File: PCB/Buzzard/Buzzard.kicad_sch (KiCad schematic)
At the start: 69 parts, among them J1 PJ-320A, J2 SDA, J3 SCL, J4 Haptic Buzz, J5 TrackPoint, J6 OLED, J7 LCD, J8 Battery, SW1 SW_DPST_x2, SW2 Reset, U1 ProMicro

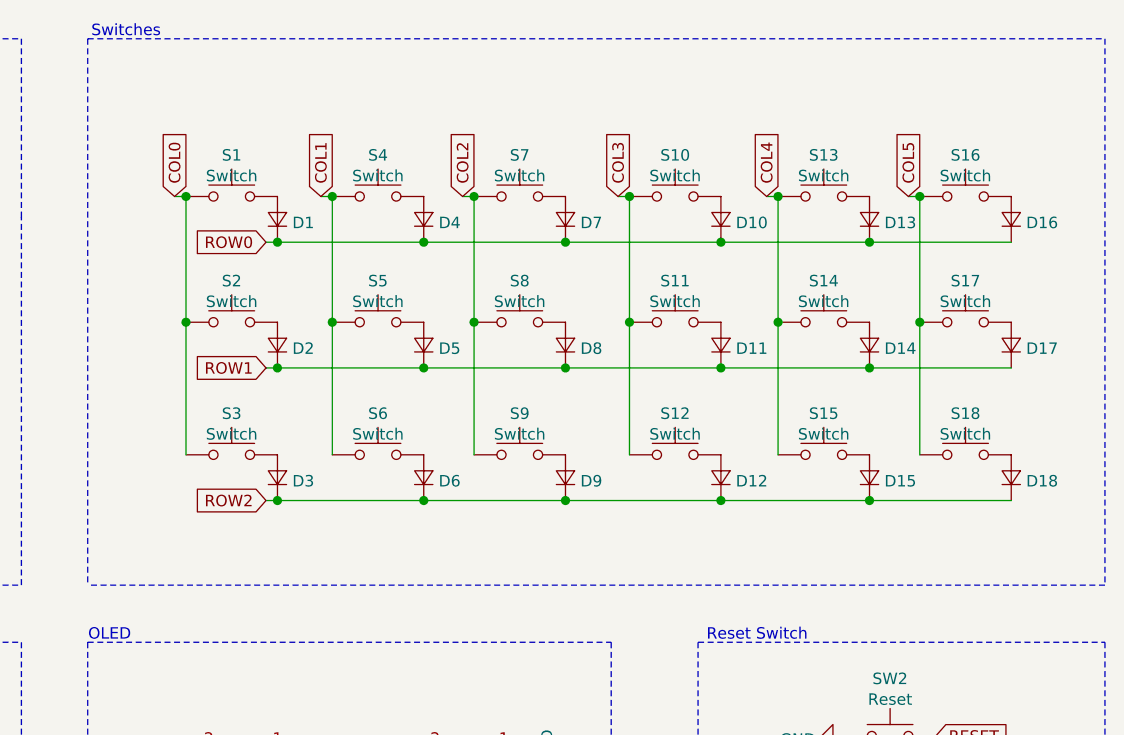
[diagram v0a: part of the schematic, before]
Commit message: started with pcb design and placed switches
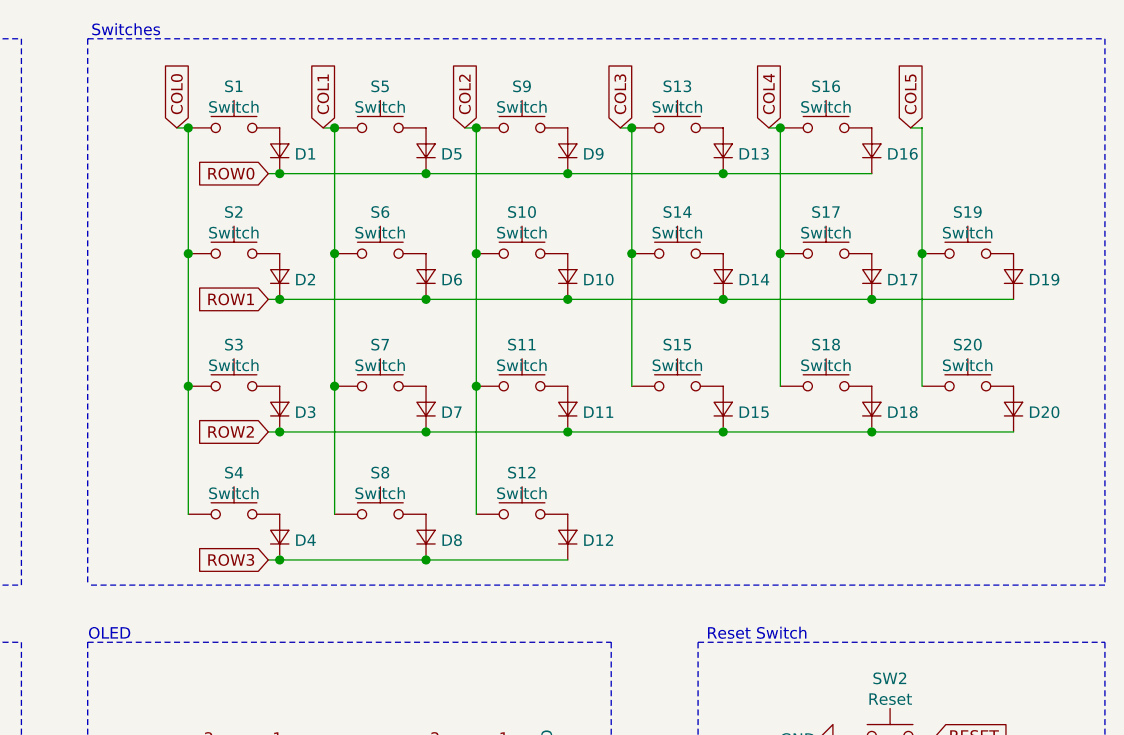
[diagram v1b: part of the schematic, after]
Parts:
- removed D18: D_Small, Buzzard:D3_TH_SMD_v2, symbol Device:D_Small
- removed S18: Switch, Buzzard:Kailh_socket_PG1350_optional_reversible.kicad_mod, symbol Switch:SW_Push
- added D12, D4, D8: D_Small, Buzzard:D3_TH_SMD_v2, symbol Device:D_Small
- added S12, S4, S8: Switch, Buzzard:Kailh_socket_PG1350_optional_reversible.kicad_mod, symbol Switch:SW_Push
- renumbered D8 to D10, D9 to D11, D10 to D13, D11 to D14, D12 to D15, D13 to D16, D14 to D17, D15 to D18, D16 to D19, D17 to D20, D4 to D5, D5 to D6, D6 to D7, D7 to D9, S8 to S10, S9 to S11, S10 to S13, S11 to S14, S12 to S15, S13 to S16, S14 to S17, S15 to S18, S16 to S19, S17 to S20, S4 to S5, S5 to S6, S6 to S7, S7 to S9
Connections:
- net COL0: now also S4.1
- net COL1: now also S8.1
- net COL2: now also S12.1
- net ROW0: no longer D19.1 (K)
- net ROW1: now also D19.1 (K); no longer D20.1 (K)
- net ROW2: now also D20.1 (K)
- net ROW3: now also D12.1 (K), D4.1 (K), D8.1 (K)
- new net: D8.2 (A), S8.2
- new net: D4.2 (A), S4.2
- new net: D12.2 (A), S12.2
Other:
- moved on the sheet: D1, D10, D11, D13, D14, D15, D16, D17, D18, D19, D2, D20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

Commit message: further work on pcb
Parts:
- J4: footprint Connector_PinHeader_1.00mm:PinHeader_1x05_P1.00mm_Vertical -> Buzzard:Pimoroni Haptic Buzz DRV2605L Driver
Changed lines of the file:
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@@
       (effects (font (size 1.27 1.27)) (justify left))
     )
-    (property "Footprint" "Connector_PinHeader_1.00mm:PinHeader_1x05_P1.00mm_Vertical" (id 2) (at 77.978 170.18 0)
+    (property "Footprint" "Buzzard:Pimoroni Haptic Buzz DRV2605L Driver" (id 2) (at 77.978 170.18 0)
       (effects (font (size 1.27 1.27)) hide)
     )
@@
     )
     (path "/15f956f5-7f0a-47a7-8d82-945c44e3054e"
-      (reference "J4") (unit 1) (value "Haptic Buzz") (footprint "Connector_PinHeader_1.00mm:PinHeader_1x05_P1.00mm_Vertical")
+      (reference "J4") (unit 1) (value "Haptic Buzz") (footprint "Buzzard:Pimoroni Haptic Buzz DRV2605L Driver")
     )
     (path "/c9007f78-8c46-454a-961b-6abc2490a937"

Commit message: further work on the pcb
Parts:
- removed J2: SDA, Connector_PinHeader_2.54mm:PinHeader_1x01_P2.54mm_Vertical, symbol Connector_Generic:Conn_01x01
- removed J3: SCL, Connector_PinHeader_2.54mm:PinHeader_1x01_P2.54mm_Vertical, symbol Connector_Generic:Conn_01x01
- removed J7: LCD, Connector_PinHeader_1.00mm:PinHeader_1x08_P1.00mm_Vertical, symbol Connector_Generic:Conn_01x09
- added J7: Sharp Memory LCD Breakout, Buzzard:SharpMemoryLcdBreakout-Reversable, symbol Connector_Generic:Conn_02x03_Odd_Even
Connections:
- net GND: now also J7.2 (Pin_2), J7.6 (Pin_6)
- net LCD_DI: now also J7.3 (Pin_3)
- net VCC: now also J7.4 (Pin_4)
- net at JP11.2 (B), JP12.2 (B): now also J7.5 (Pin_5)
- net at JP10.2 (B), JP9.2 (B): now also J7.1 (Pin_1)
- no-connect marks 2 -> 0

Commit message: further work
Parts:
- J7: symbol Connector_Generic:Conn_02x03_Odd_Even -> Connector_Generic:Conn_2Rows-05Pins
- S1, S10, S5, S6, S9: footprint Buzzard:Kailh_socket_PG1350_optional_reversible.kicad_mod -> Buzzard:SW_PG1350_reversible
- SW2: footprint Buzzard:SMD-SW-4_5.1x5.1x2.5 -> Buzzard:SW_Tactile_SPST_Angled_PTS645Vx39-2LFS
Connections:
- net GND: no longer J7.6 (Pin_6)
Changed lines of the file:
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@@
-    (pin "1")
-  )
-  (symbol (lib_id "power:GND") (at 159.004 171.45 90) (unit 1)
-    (in_bom yes) (on_board yes) (fields_autoplaced)
-    (property "Reference" "#PWR0101" (id 0) (at 165.354 171.45 0)
-      (effects (font (size 1.27 1.27)) hide)
-    )
-    (property "Value" "GND" (id 1) (at 162.1791 171.8385 90)
-      (effects (font (size 1.27 1.27)) (justify right))
-    )
-    (property "Footprint" "" (id 2) (at 159.004 171.45 0)
-      (effects (font (size 1.27 1.27)) hide)
-    )
-    (property "Datasheet" "" (id 3) (at 159.004 171.45 0)
-      (effects (font (size 1.27 1.27)) hide)
-    )
     (pin "1")
   )
@@
   (symbol (lib_id "Switch:SW_Push") (at 129.54 26.162 0) (unit 1)
     (in_bom yes) (on_board yes) (fields_autoplaced)
-    (property "Reference" "S1" (id 0) (at 129.54 21.5858 0))
-    (property "Value" "Switch" (id 1) (at 129.54 23.8845 0))
-    (property "Footprint" "Buzzard:Kailh_socket_PG1350_optional_reversible.kicad_mod" (id 2) (at 129.54 21.082 0)
+    (property "Reference" "S1" (id 0) (at 129.54 19.8078 0))
+    (property "Value" "Switch" (id 1) (at 129.54 22.1065 0))
+    (property "Footprint" "Buzzard:SW_PG1350_reversible" (id 2) (at 129.54 21.082 0)
       (effects (font (size 1.27 1.27)) hide)
     )
@@
     (property "Reference" "S5" (id 0) (at 145.796 21.5858 0))
     (property "Value" "Switch" (id 1) (at 145.796 23.8845 0))
-    (property "Footprint" "Buzzard:Kailh_socket_PG1350_optional_reversible.kicad_mod" (id 2) (at 145.796 21.082 0)
+    (property "Footprint" "Buzzard:SW_PG1350_reversible" (id 2) (at 145.796 21.082 0)
       (effects (font (size 1.27 1.27)) hide)
     )
@@
     (property "Reference" "S6" (id 0) (at 145.796 35.5558 0))
     (property "Value" "Switch" (id 1) (at 145.796 37.8545 0))
-    (property "Footprint" "Buzzard:Kailh_socket_PG1350_optional_reversible.kicad_mod" (id 2) (at 145.796 35.052 0)
+    (property "Footprint" "Buzzard:SW_PG1350_reversible" (id 2) (at 145.796 35.052 0)
       (effects (font (size 1.27 1.27)) hide)
     )
@@
     (property "Reference" "S9" (id 0) (at 161.544 21.5858 0))
     (property "Value" "Switch" (id 1) (at 161.544 23.8845 0))
-    (property "Footprint" "Buzzard:Kailh_socket_PG1350_optional_reversible.kicad_mod" (id 2) (at 161.544 21.082 0)
+    (property "Footprint" "Buzzard:SW_PG1350_reversible" (id 2) (at 161.544 21.082 0)
       (effects (font (size 1.27 1.27)) hide)
     )
@@
     (property "Reference" "S10" (id 0) (at 161.544 35.5558 0))
     (property "Value" "Switch" (id 1) (at 161.544 37.8545 0))
-    (property "Footprint" "Buzzard:Kailh_socket_PG1350_optional_reversible.kicad_mod" (id 2) (at 161.544 35.052 0)
+    (property "Footprint" "Buzzard:SW_PG1350_reversible" (id 2) (at 161.544 35.052 0)
       (effects (font (size 1.27 1.27)) hide)
     )
@@
     (property "Reference" "SW2" (id 0) (at 202.438 87.3718 0))
     (property "Value" "Reset" (id 1) (at 202.438 89.6705 0))
-    (property "Footprint" "Buzzard:SMD-SW-4_5.1x5.1x2.5" (id 2) (at 202.438 88.646 0)
+    (property "Footprint" "Buzzard:SW_Tactile_SPST_Angled_PTS645Vx39-2LFS" (id 2) (at 202.438 88.646 0)
       (effects (font (size 1.27 1.27)) hide)
     )
@@
     (pin "5")
   )
-  (symbol (lib_id "Connector_Generic:Conn_02x03_Odd_Even") (at 151.384 168.91 0) (unit 1)
+  (symbol (lib_id "Connector_Generic:Conn_2Rows-05Pins") (at 151.384 168.91 0) (unit 1)
     (in_bom yes) (on_board yes)
     (property "Reference" "J7" (id 0) (at 152.654 161.6668 0))
@@
     (pin "4")
     (pin "5")
-    (pin "6")
   )
   (symbol (lib_id "Connector:AudioJack4") (at 42.418 95.25 0) (unit 1)
@@
       (reference "#PWR021") (unit 1) (value "GND") (footprint "")
     )
-    (path "/dbdd680f-63ed-49ac-889b-761f7ea73750"
-      (reference "#PWR0101") (unit 1) (value "GND") (footprint "")
-    )
     (path "/c869f587-3433-4e49-b864-4e64391cc97e"
       (reference "C1") (unit 1) (value "2.2uF") (footprint "Buzzard:C_THT_SMD_0805_HandSolder_Reversable")
@@
     )
     (path "/9cdf4502-752b-4f55-b9dd-3b2cc7b72863"
-      (reference "S1") (unit 1) (value "Switch") (footprint "Buzzard:Kailh_socket_PG1350_optional_reversible.kicad_mod")
+      (reference "S1") (unit 1) (value "Switch") (footprint "Buzzard:SW_PG1350_reversible")
     )
     (path "/0c45afcd-84c4-449f-8c55-610232e591cb"
@@
     )
     (path "/c425926d-042f-4d4a-bd5e-405bf1c02c13"
-      (reference "S5") (unit 1) (value "Switch") (footprint "Buzzard:Kailh_socket_PG1350_optional_reversible.kicad_mod")
+      (reference "S5") (unit 1) (value "Switch") (footprint "Buzzard:SW_PG1350_reversible")
     )
     (path "/caecacf4-cc4d-41e2-b156-a7301cb858f8"
-      (reference "S6") (unit 1) (value "Switch") (footprint "Buzzard:Kailh_socket_PG1350_optional_reversible.kicad_mod")
+      (reference "S6") (unit 1) (value "Switch") (footprint "Buzzard:SW_PG1350_reversible")
     )
     (path "/13477fde-7f3f-473f-a644-65c174cf4bad"
@@
     )
     (path "/0947da5b-4663-413e-b90b-85b23856db74"
-      (reference "S9") (unit 1) (value "Switch") (footprint "Buzzard:Kailh_socket_PG1350_optional_reversible.kicad_mod")
+      (reference "S9") (unit 1) (value "Switch") (footprint "Buzzard:SW_PG1350_reversible")
     )
     (path "/cc90187a-182f-4f68-9243-0893db8e7cd6"
-      (reference "S10") (unit 1) (value "Switch") (footprint "Buzzard:Kailh_socket_PG1350_optional_reversible.kicad_mod")
+      (reference "S10") (unit 1) (value "Switch") (footprint "Buzzard:SW_PG1350_reversible")
     )
     (path "/c3e4d536-ac79-49eb-8d4f-6dc2f37db51e"
@@
     )
     (path "/bf95f5bc-33d3-4423-aea8-d2265c13afb5"
-      (reference "SW2") (unit 1) (value "Reset") (footprint "Buzzard:SMD-SW-4_5.1x5.1x2.5")
+      (reference "SW2") (unit 1) (value "Reset") (footprint "Buzzard:SW_Tactile_SPST_Angled_PTS645Vx39-2LFS")
     )
     (path "/93b725f9-a829-4065-94f0-79a40216db8d"

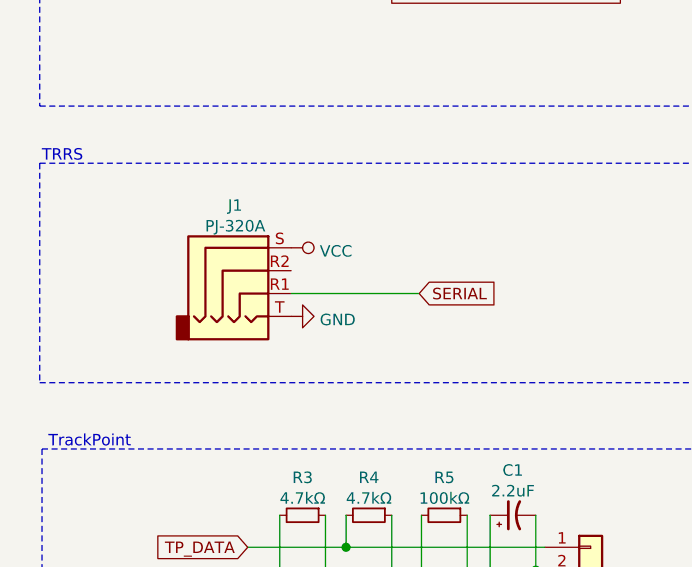
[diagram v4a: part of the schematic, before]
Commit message: replaced trrs symbol and fixed connections
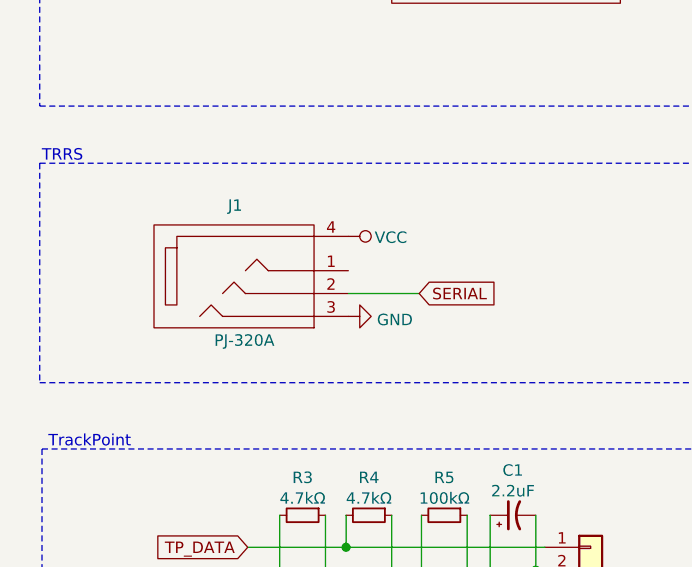
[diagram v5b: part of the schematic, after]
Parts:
- J1: symbol Connector:AudioJack4 -> Buzzard:MJ-4PP-9
- J5: footprint Connector_PinHeader_1.00mm:PinHeader_1x05_P1.00mm_Vertical -> Connector_PinHeader_2.54mm:PinHeader_1x05_P2.54mm_Vertical
- J8: footprint Connector_JST:JST_PH_B2B-PH-K_1x02_P2.00mm_Vertical -> Connector_JST:JST_PH_S2B-PH-K_1x02_P2.00mm_Horizontal
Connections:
- net GND: now also J1.3; no longer J1.T
- net SERIAL: now also J1.2; no longer J1.R1
- net VCC: now also J1.4; no longer J1.S
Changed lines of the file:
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@@
-    (stroke (width 0) (type solid) (color 0 0 0 0))
-  )
-  (wire (pts (xy 47.498 97.79) (xy 61.722 97.79))
     (stroke (width 0) (type solid) (color 0 0 0 0))
   )
@@
   )
   (wire (pts (xy 53.594 125.984) (xy 75.692 125.984))
+    (stroke (width 0) (type solid) (color 0 0 0 0))
+  )
+  (wire (pts (xy 53.848 97.79) (xy 61.722 97.79))
     (stroke (width 0) (type solid) (color 0 0 0 0))
   )
@@
     (pin "1")
   )
-  (symbol (lib_id "power:VCC") (at 47.498 92.71 270) (unit 1)
-    (in_bom yes) (on_board yes) (fields_autoplaced)
-    (property "Reference" "#PWR09" (id 0) (at 43.688 92.71 0)
-      (effects (font (size 1.27 1.27)) hide)
-    )
-    (property "Value" "VCC" (id 1) (at 50.6731 93.0985 90)
-      (effects (font (size 1.27 1.27)) (justify left))
-    )
-    (property "Footprint" "" (id 2) (at 47.498 92.71 0)
-      (effects (font (size 1.27 1.27)) hide)
-    )
-    (property "Datasheet" "" (id 3) (at 47.498 92.71 0)
+  (symbol (lib_id "power:VCC") (at 53.848 91.44 270) (unit 1)
+    (in_bom yes) (on_board yes)
+    (property "Reference" "#PWR09" (id 0) (at 50.038 91.44 0)
+      (effects (font (size 1.27 1.27)) hide)
+    )
+    (property "Value" "VCC" (id 1) (at 56.7691 91.5745 90)
+      (effects (font (size 1.27 1.27)) (justify left))
+    )
+    (property "Footprint" "" (id 2) (at 53.848 91.44 0)
+      (effects (font (size 1.27 1.27)) hide)
+    )
+    (property "Datasheet" "" (id 3) (at 53.848 91.44 0)
       (effects (font (size 1.27 1.27)) hide)
     )
@@
     (pin "1")
   )
-  (symbol (lib_id "power:GND") (at 47.498 100.33 90) (unit 1)
-    (in_bom yes) (on_board yes) (fields_autoplaced)
-    (property "Reference" "#PWR010" (id 0) (at 53.848 100.33 0)
-      (effects (font (size 1.27 1.27)) hide)
-    )
-    (property "Value" "GND" (id 1) (at 50.6731 100.7185 90)
-      (effects (font (size 1.27 1.27)) (justify right))
-    )
-    (property "Footprint" "" (id 2) (at 47.498 100.33 0)
-      (effects (font (size 1.27 1.27)) hide)
-    )
-    (property "Datasheet" "" (id 3) (at 47.498 100.33 0)
-      (effects (font (size 1.27 1.27)) hide)
-    )
-    (pin "1")
-  )
   (symbol (lib_id "power:GND") (at 51.562 41.402 270) (unit 1)
     (in_bom yes) (on_board yes) (fields_autoplaced)
@@
     )
     (property "Datasheet" "" (id 3) (at 51.562 41.402 0)
+      (effects (font (size 1.27 1.27)) hide)
+    )
+    (pin "1")
+  )
+  (symbol (lib_id "power:GND") (at 53.848 100.33 90) (unit 1)
+    (in_bom yes) (on_board yes) (fields_autoplaced)
+    (property "Reference" "#PWR010" (id 0) (at 60.198 100.33 0)
+      (effects (font (size 1.27 1.27)) hide)
+    )
+    (property "Value" "GND" (id 1) (at 57.0231 100.7185 90)
+      (effects (font (size 1.27 1.27)) (justify right))
+    )
+    (property "Footprint" "" (id 2) (at 53.848 100.33 0)
+      (effects (font (size 1.27 1.27)) hide)
+    )
+    (property "Datasheet" "" (id 3) (at 53.848 100.33 0)
       (effects (font (size 1.27 1.27)) hide)
     )
@@
       (effects (font (size 1.27 1.27)) (justify left))
     )
-    (property "Footprint" "Connector_JST:JST_PH_B2B-PH-K_1x02_P2.00mm_Vertical" (id 2) (at 209.296 109.982 0)
+    (property "Footprint" "Connector_JST:JST_PH_S2B-PH-K_1x02_P2.00mm_Horizontal" (id 2) (at 209.296 109.982 0)
       (effects (font (size 1.27 1.27)) hide)
     )
@@
       (effects (font (size 1.27 1.27)) (justify left))
     )
-    (property "Footprint" "Connector_PinHeader_1.00mm:PinHeader_1x05_P1.00mm_Vertical" (id 2) (at 80.772 131.064 0)
+    (property "Footprint" "Connector_PinHeader_2.54mm:PinHeader_1x05_P2.54mm_Vertical" (id 2) (at 80.772 131.064 0)
       (effects (font (size 1.27 1.27)) hide)
     )
@@
     (pin "5")
   )
-  (symbol (lib_id "Connector:AudioJack4") (at 42.418 95.25 0) (unit 1)
-    (in_bom yes) (on_board yes) (fields_autoplaced)
+  (symbol (lib_id "Buzzard:MJ-4PP-9") (at 42.418 95.25 0) (unit 1)
+    (in_bom yes) (on_board yes)
     (property "Reference" "J1" (id 0) (at 41.275 88.0068 0))
-    (property "Value" "PJ-320A" (id 1) (at 41.275 90.3055 0))
+    (property "Value" "PJ-320A" (id 1) (at 42.291 103.0055 0))
     (property "Footprint" "Buzzard:MJ-4PP-9" (id 2) (at 42.418 95.25 0)
       (effects (font (size 1.27 1.27)) hide)
@@
       (effects (font (size 1.27 1.27)) hide)
     )
-    (pin "R1")
-    (pin "R2")
-    (pin "S")
-    (pin "T")
+    (pin "1")
+    (pin "2")
+    (pin "3")
+    (pin "4")
   )
   (symbol (lib_id "Buzzard:ProMicro") (at 71.374 49.022 0) (unit 1)
@@
     )
     (path "/c9007f78-8c46-454a-961b-6abc2490a937"
-      (reference "J5") (unit 1) (value "TrackPoint") (footprint "Connector_PinHeader_1.00mm:PinHeader_1x05_P1.00mm_Vertical")
+      (reference "J5") (unit 1) (value "TrackPoint") (footprint "Connector_PinHeader_2.54mm:PinHeader_1x05_P2.54mm_Vertical")
     )
     (path "/08af2616-c5f2-4d06-a067-6eb412a99e32"
@@
     )
     (path "/2f8434cd-6d39-4f1d-b665-ce1d98700990"
-      (reference "J8") (unit 1) (value "Battery") (footprint "Connector_JST:JST_PH_B2B-PH-K_1x02_P2.00mm_Vertical")
+      (reference "J8") (unit 1) (value "Battery") (footprint "Connector_JST:JST_PH_S2B-PH-K_1x02_P2.00mm_Horizontal")
     )
     (path "/cf3979ae-0df8-494d-8c6e-667727ffd702"
